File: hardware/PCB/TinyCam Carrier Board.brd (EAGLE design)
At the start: 160 x 100 mm, 8 parts, among them J1 694102303002, Q1 IRLB8721PBF

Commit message: Updated PCB layout to accomodate for SD card slot
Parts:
- moved S1 16.6 mm to (72.4, 38.1), turned to 90 degrees
- moved J1 15.2 mm to (72.4, 19.1)
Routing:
- net VUSB: track 117.1 -> 100.1 mm
- net GND: track 81.3 -> 66.1 mm
- net BJ_VIN: track 10.4 -> 19.5 mm
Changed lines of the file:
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@@
 <text x="10.16" y="43.18" size="1.778" layer="25">Boron</text>
 <text x="43.18" y="43.18" size="1.778" layer="25">OpenMV</text>
-<text x="68.58" y="27.94" size="1.778" layer="27">ON</text>
-<text x="73.66" y="15.24" size="1.778" layer="27" rot="R180">OFF</text>
+<text x="71.12" y="35.56" size="1.778" layer="27" rot="R180">ON</text>
+<text x="78.74" y="35.56" size="1.778" layer="27" rot="R180">OFF</text>
 <hole x="71.12" y="43.18" drill="3"/>
 <hole x="5.08" y="5.08" drill="3"/>
@@
 <attribute name="VALUE" x="8.255" y="13.97" size="1.27" layer="27" rot="R90"/>
 </element>
-<element name="J1" library="Eagle_WR-DC (rev21a)" package="694102303002" package3d_urn="urn:adsk.eagle:package:14886064/3" value=" 694102303002 " x="72.39" y="34.29" smashed="yes" rot="R180">
-<attribute name="DATASHEET-URL" value="https://www.we-online.com/catalog/datasheet/694102303002.pdf" x="40.64" y="40.64" size="1.778" layer="27" rot="R180" display="off"/>
-<attribute name="IR" value="2A" x="40.64" y="40.64" size="1.778" layer="27" rot="R180" display="off"/>
-<attribute name="MOUNT" value="THT" x="40.64" y="40.64" size="1.778" layer="27" rot="R180" display="off"/>
-<attribute name="NAME" x="77.47" y="37.79" size="1.27" layer="25" ratio="13" rot="SR0" align="bottom-center"/>
-<attribute name="PART-NUMBER" value=" 694102303002 " x="40.64" y="40.64" size="1.778" layer="27" rot="R180" display="off"/>
-<attribute name="TYPE" value="Right Angled" x="40.64" y="40.64" size="1.778" layer="27" rot="R180" display="off"/>
-<attribute name="WORKING-VOLTAGE" value="30V(AC)" x="40.64" y="40.64" size="1.778" layer="27" rot="R180" display="off"/>
+<element name="J1" library="Eagle_WR-DC (rev21a)" package="694102303002" package3d_urn="urn:adsk.eagle:package:14886064/3" value=" 694102303002 " x="72.39" y="19.05" smashed="yes" rot="R180">
+<attribute name="DATASHEET-URL" value="https://www.we-online.com/catalog/datasheet/694102303002.pdf" x="40.64" y="25.4" size="1.778" layer="27" rot="R180" display="off"/>
+<attribute name="IR" value="2A" x="40.64" y="25.4" size="1.778" layer="27" rot="R180" display="off"/>
+<attribute name="MOUNT" value="THT" x="40.64" y="25.4" size="1.778" layer="27" rot="R180" display="off"/>
+<attribute name="NAME" x="77.47" y="22.55" size="1.27" layer="25" ratio="13" rot="SR0" align="bottom-center"/>
+<attribute name="PART-NUMBER" value=" 694102303002 " x="40.64" y="25.4" size="1.778" layer="27" rot="R180" display="off"/>
+<attribute name="TYPE" value="Right Angled" x="40.64" y="25.4" size="1.778" layer="27" rot="R180" display="off"/>
+<attribute name="WORKING-VOLTAGE" value="30V(AC)" x="40.64" y="25.4" size="1.778" layer="27" rot="R180" display="off"/>
 </element>
 <element name="OMV_LEFT_HEADER" library="con-lsta" library_urn="urn:adsk.eagle:library:161" package="FE08" package3d_urn="urn:adsk.eagle:package:8194/1" value="" x="33.02" y="13.97" smashed="yes" rot="R90">
@@
 <attribute name="VALUE" x="66.721" y="3.81" size="1.27" layer="27" ratio="10" rot="R90"/>
 </element>
-<element name="S1" library="Switch" library_urn="urn:adsk.eagle:library:16378657" package="DS-01" package3d_urn="urn:adsk.eagle:package:38918339/1" value="DS-01" x="71.12" y="21.59" smashed="yes">
-<attribute name="CATEGORY" value="SWITCH" x="87.63" y="13.97" size="1.778" layer="27" display="off"/>
-<attribute name="DESCRIPTION" value="" x="87.63" y="13.97" size="1.778" layer="27" display="off"/>
-<attribute name="MANUFACTURER" value="" x="87.63" y="13.97" size="1.778" layer="27" display="off"/>
-<attribute name="MPN" value="" x="87.63" y="13.97" size="1.778" layer="27" display="off"/>
-<attribute name="NAME" x="72.898" y="27.051" size="1.27" layer="25" ratio="10"/>
-<attribute name="OPERATING_TEMP" value="" x="87.63" y="13.97" size="1.778" layer="27" display="off"/>
-<attribute name="PART_STATUS" value="" x="87.63" y="13.97" size="1.778" layer="27" display="off"/>
-<attribute name="ROHS_COMPLIANT" value="" x="87.63" y="13.97" size="1.778" layer="27" display="off"/>
-<attribute name="SERIES" value="" x="87.63" y="13.97" size="1.778" layer="27" display="off"/>
-<attribute name="SUB-CATEGORY" value="" x="87.63" y="13.97" size="1.778" layer="27" display="off"/>
-<attribute name="THERMALLOSS" value="" x="87.63" y="13.97" size="1.778" layer="27" display="off"/>
-<attribute name="TYPE" value="SPST" x="87.63" y="13.97" size="1.778" layer="27" display="off"/>
+<element name="S1" library="Switch" library_urn="urn:adsk.eagle:library:16378657" package="DS-01" package3d_urn="urn:adsk.eagle:package:38918339/1" value="DS-01" x="72.39" y="38.1" smashed="yes" rot="R90">
+<attribute name="CATEGORY" value="SWITCH" x="80.01" y="54.61" size="1.778" layer="27" rot="R90" display="off"/>
+<attribute name="DESCRIPTION" value="" x="80.01" y="54.61" size="1.778" layer="27" rot="R90" display="off"/>
+<attribute name="MANUFACTURER" value="" x="80.01" y="54.61" size="1.778" layer="27" rot="R90" display="off"/>
+<attribute name="MPN" value="" x="80.01" y="54.61" size="1.778" layer="27" rot="R90" display="off"/>
+<attribute name="NAME" x="66.929" y="39.878" size="1.27" layer="25" ratio="10" rot="R90"/>
+<attribute name="OPERATING_TEMP" value="" x="80.01" y="54.61" size="1.778" layer="27" rot="R90" display="off"/>
+<attribute name="PART_STATUS" value="" x="80.01" y="54.61" size="1.778" layer="27" rot="R90" display="off"/>
+<attribute name="ROHS_COMPLIANT" value="" x="80.01" y="54.61" size="1.778" layer="27" rot="R90" display="off"/>
+<attribute name="SERIES" value="" x="80.01" y="54.61" size="1.778" layer="27" rot="R90" display="off"/>
+<attribute name="SUB-CATEGORY" value="" x="80.01" y="54.61" size="1.778" layer="27" rot="R90" display="off"/>
+<attribute name="THERMALLOSS" value="" x="80.01" y="54.61" size="1.778" layer="27" rot="R90" display="off"/>
+<attribute name="TYPE" value="SPST" x="80.01" y="54.61" size="1.778" layer="27" rot="R90" display="off"/>
 </element>
 <element name="Q1" library="IRLB8721PBF" package="TO254P1067X483X2057-3" value="IRLB8721PBF" x="71.12" y="7.62" smashed="yes" rot="R90">
@@
 <wire x1="76.2" y1="11.43" x2="72.39" y2="11.43" width="0.1524" layer="16"/>
 <wire x1="72.39" y1="11.43" x2="71.12" y2="10.16" width="0.1524" layer="16"/>
-<wire x1="72.39" y1="34.29" x2="70.09" y2="36.59" width="0.1524" layer="16"/>
-<wire x1="70.09" y1="36.59" x2="70.09" y2="37.09" width="0.1524" layer="16"/>
-<wire x1="76.2" y1="11.43" x2="76.2" y2="30.48" width="0.1524" layer="16"/>
-<wire x1="76.2" y1="30.48" x2="72.39" y2="34.29" width="0.1524" layer="16"/>
 <wire x1="25.4" y1="12.7" x2="31.1023625" y2="12.7" width="0.1524" layer="16"/>
 <wire x1="31.1023625" y1="12.7" x2="31.9913625" y2="13.589" width="0.1524" layer="16"/>
 <wire x1="31.9913625" y1="13.589" x2="67.691" y2="13.589" width="0.1524" layer="16"/>
 <wire x1="67.691" y1="13.589" x2="71.12" y2="10.16" width="0.1524" layer="16"/>
+<wire x1="70.09" y1="21.85" x2="72.39" y2="19.55" width="0.1524" layer="16"/>
+<wire x1="72.39" y1="19.55" x2="72.39" y2="19.05" width="0.1524" layer="16"/>
+<wire x1="76.2" y1="11.43" x2="72.39" y2="15.24" width="0.1524" layer="16"/>
+<wire x1="72.39" y1="15.24" x2="72.39" y2="19.05" width="0.1524" layer="16"/>
 </signal>
 <signal name="TX">
@@
 <contactref element="OMV_RIGHT_HEADER" pad="2"/>
 <wire x1="5.08" y1="20.32" x2="5.08" y2="20.697075" width="0.1524" layer="1"/>
-<wire x1="5.08" y1="20.697075" x2="3.3274" y2="22.449675" width="0.1524" layer="1"/>
-<wire x1="3.3274" y1="43.590325" x2="5.08" y2="45.342925" width="0.1524" layer="1"/>
-<wire x1="3.3274" y1="22.449675" x2="3.3274" y2="43.590325" width="0.1524" layer="1"/>
-<wire x1="5.08" y1="45.342925" x2="43.557075" y2="45.342925" width="0.1524" layer="1"/>
-<wire x1="43.557075" y1="45.342925" x2="71.12" y2="17.78" width="0.1524" layer="1"/>
-<wire x1="63.8" y1="7.62" x2="71.12" y2="14.94" width="0.1524" layer="1"/>
-<wire x1="71.12" y1="14.94" x2="71.12" y2="17.78" width="0.1524" layer="1"/>
+<wire x1="76.2" y1="38.1" x2="76.2" y2="20.02" width="0.1524" layer="1"/>
+<wire x1="76.2" y1="20.02" x2="63.8" y2="7.62" width="0.1524" layer="1"/>
+<wire x1="26.673925" y1="16.891" x2="26.572325" y2="16.7894" width="0.1524" layer="1"/>
+<wire x1="26.572325" y1="16.7894" x2="8.6106" y2="16.7894" width="0.1524" layer="1"/>
+<wire x1="8.6106" y1="16.7894" x2="5.08" y2="20.32" width="0.1524" layer="1"/>
+<wire x1="33.909" y1="16.891" x2="26.673925" y2="16.891" width="0.1524" layer="1"/>
+<wire x1="33.909" y1="16.891" x2="54.529" y2="16.891" width="0.1524" layer="1"/>
+<wire x1="54.529" y1="16.891" x2="63.8" y2="7.62" width="0.1524" layer="1"/>
 </signal>
 <signal name="D8">
@@
 <contactref element="J1" pad="1"/>
 <contactref element="S1" pad="2"/>
-<wire x1="71.12" y1="25.4" x2="67.49" y2="29.03" width="0.1524" layer="1"/>
-<wire x1="67.49" y1="29.03" x2="67.49" y2="34.29" width="0.1524" layer="1"/>
+<wire x1="67.49" y1="19.05" x2="67.49" y2="37.01" width="0.1524" layer="1"/>
+<wire x1="67.49" y1="37.01" x2="68.58" y2="38.1" width="0.1524" layer="1"/>
 </signal>
 </signals>

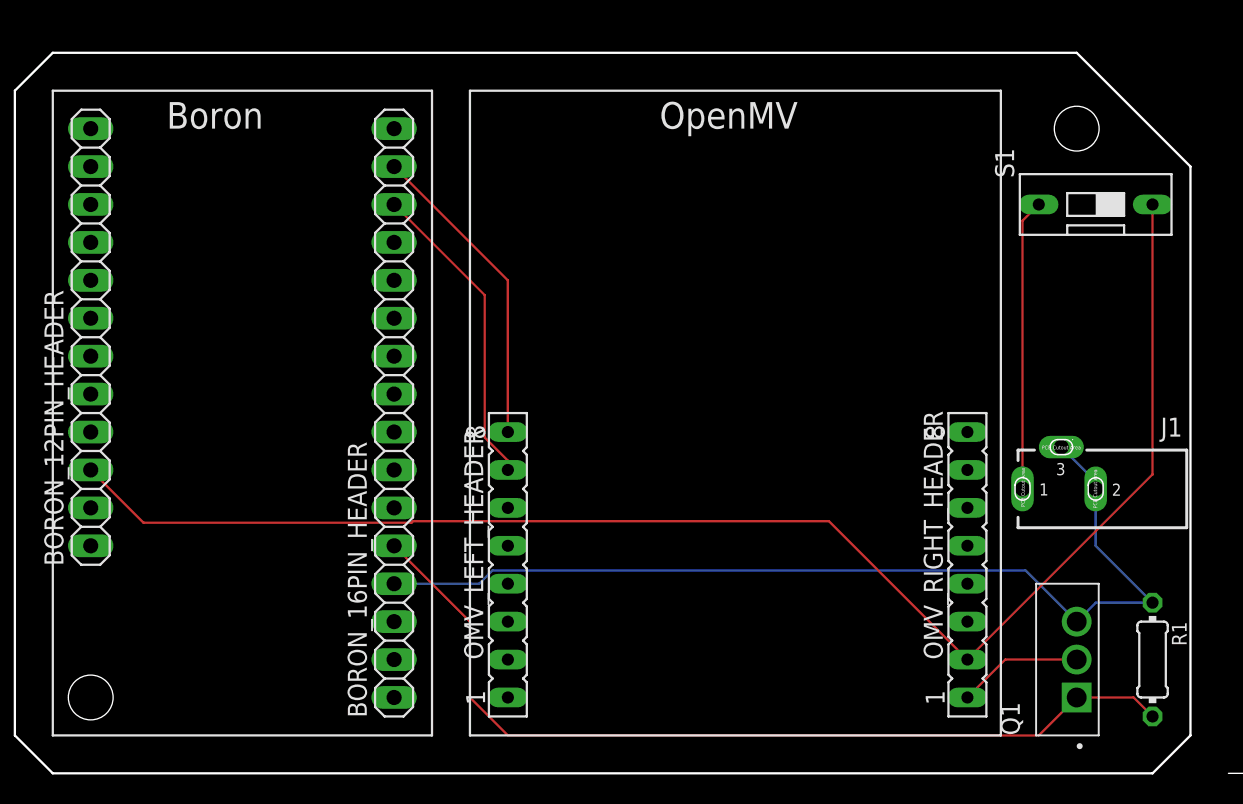
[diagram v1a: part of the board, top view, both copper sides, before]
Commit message: Fixed OpenMV pin distance
Updated board layout, brd file, and CAM data with corrected 32.26mm pin to pin distance for the OpenMV H7 Plus.
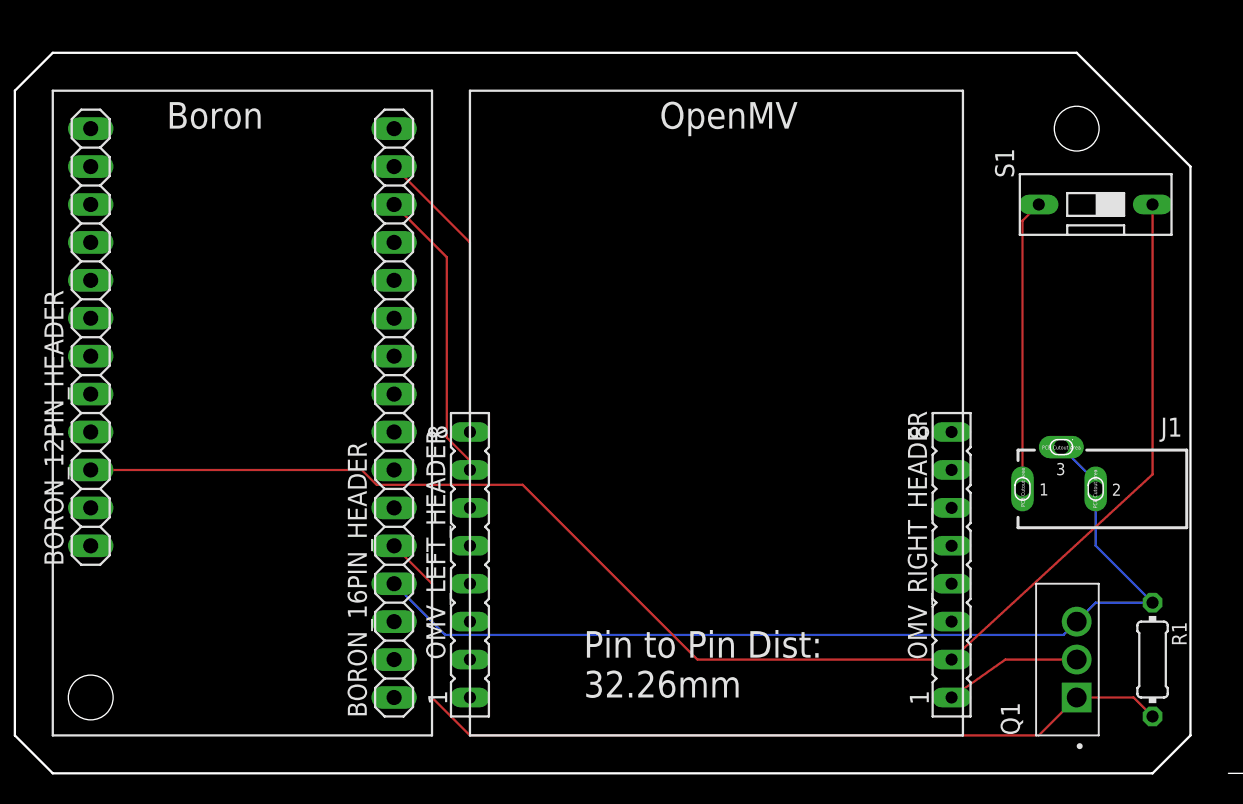
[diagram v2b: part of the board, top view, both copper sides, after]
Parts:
- moved OMV_LEFT_HEADER 2.54 mm to (30.5, 14.0)
- moved OMV_RIGHT_HEADER 1.06 mm to (62.7, 14.0)
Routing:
- net A0: track 60.6 -> 62.1 mm
- net TX: track 20.9 -> 19.9 mm
- net RX: track 20.9 -> 19.9 mm
- net OMV_GND: track 8.37 -> 9.19 mm
- net VUSB: track 100.1 -> 99.3 mm
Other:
- board text added: "Pin to Pin Dist: 32.26mm"
- board text removed: "Pin to Pin Dist 30.78mm"
